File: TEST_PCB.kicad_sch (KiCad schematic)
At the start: 21 parts, among them J101 Conn_01x07_Socket, J102 Conn_01x04_Socket, J103 Conn_01x04_Socket, J104 Conn_01x02_Socket, J105 Conn_01x04_Socket, J106 Conn_01x02_Socket, J107 Conn_01x04_Socket, J108 Conn_01x02_Socket, J109 Conn_01x02_Socket, J110 Conn_01x02_Socket, J111 Conn_01x04_Socket, J112 Conn_01x02_Socket, J113 Conn_01x04_Socket

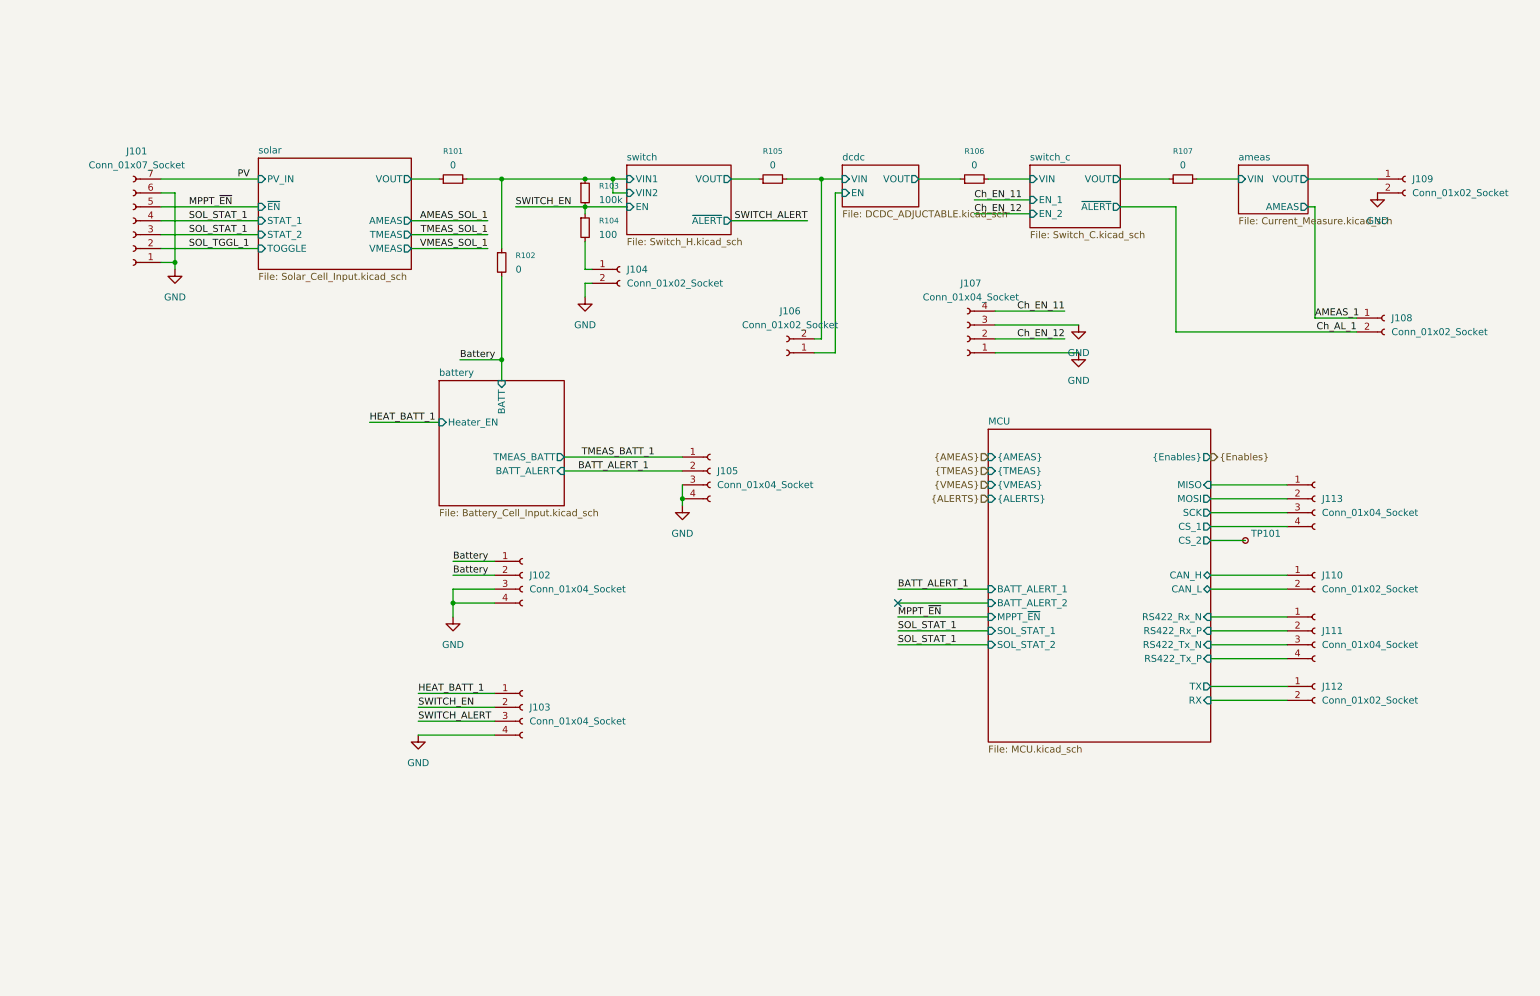
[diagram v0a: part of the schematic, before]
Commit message: reduced number of DCDC converter for PV panels; updated test pcb
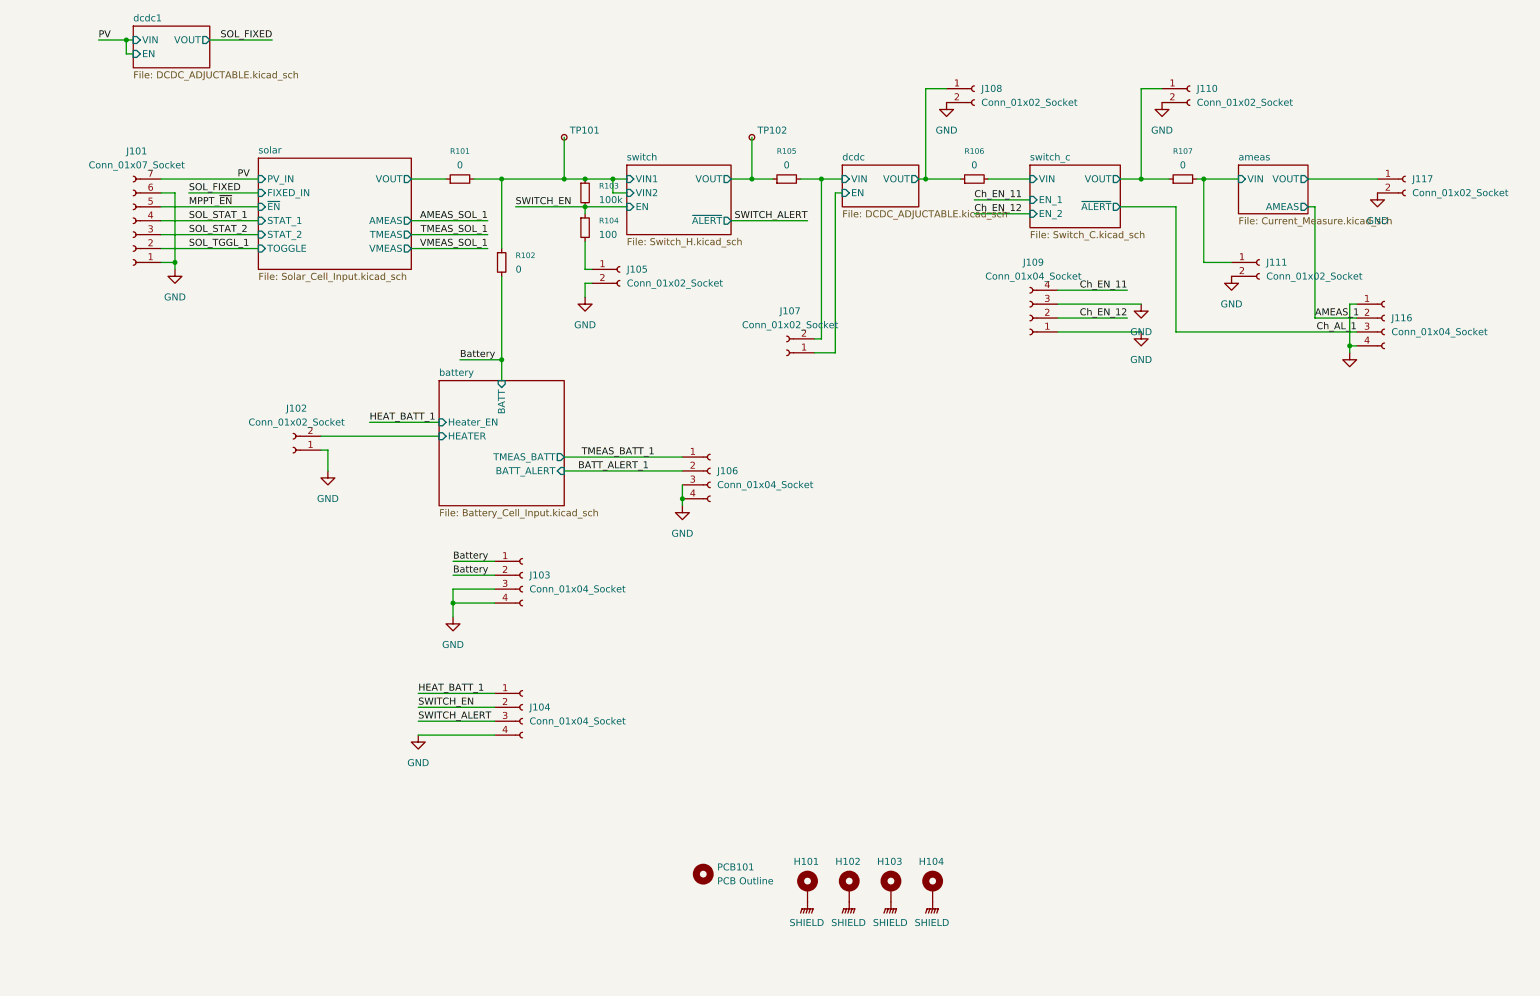
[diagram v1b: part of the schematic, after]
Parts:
- removed J111, J113: Conn_01x04_Socket, symbol Connector:Conn_01x04_Socket
- removed J112: Conn_01x02_Socket, symbol Connector:Conn_01x02_Socket
- added H101, H102, H103, H104: MountingHole, MountingHole:MountingHole_3.2mm_M3_Pad_Via, symbol Mechanical:MountingHole_Pad
- added J102, J111: Conn_01x02_Socket, Connector_PinSocket_2.54mm:PinSocket_1x02_P2.54mm_Vertical, symbol Connector:Conn_01x02_Socket
- added J116: Conn_01x04_Socket, Connector_PinSocket_2.54mm:PinSocket_1x04_P2.54mm_Vertical, symbol Connector:Conn_01x04_Socket
- added PCB101: PCB Outline, Outlines:SPACEMANIC_V1c, symbol Mechanical:MountingHole
- added TP102: ~, TestPoint:TestPoint_Pad_1.0x1.0mm, symbol Connector:TestPoint_Small
- J101: footprint (none) -> Connector_PinSocket_2.54mm:PinSocket_1x07_P2.54mm_Vertical
- J103: renamed from J102; footprint (none) -> Connector_PinSocket_2.54mm:PinSocket_1x04_P2.54mm_Vertical
- J104: renamed from J103; footprint (none) -> Connector_PinSocket_2.54mm:PinSocket_1x04_P2.54mm_Vertical
- J105: renamed from J104; footprint (none) -> Connector_PinSocket_2.54mm:PinSocket_1x02_P2.54mm_Vertical
- J106: renamed from J105; footprint (none) -> Connector_PinSocket_2.54mm:PinSocket_1x04_P2.54mm_Vertical
- J107: renamed from J106; footprint (none) -> Connector_PinSocket_2.54mm:PinSocket_1x02_P2.54mm_Vertical
- J108, J110: footprint (none) -> Connector_PinSocket_2.54mm:PinSocket_1x02_P2.54mm_Vertical
- J109: renamed from J107; footprint (none) -> Connector_PinSocket_2.54mm:PinSocket_1x04_P2.54mm_Vertical
- J117: renamed from J109; footprint (none) -> Connector_PinSocket_2.54mm:PinSocket_1x02_P2.54mm_Vertical
- R101, R102, R103, R104, R105, R106, R107: footprint (none) -> Resistor_SMD:R_0603_1608Metric_Pad0.98x0.95mm_HandSolder
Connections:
- net MCU/CAN_H is gone; now on net switch_c/VOUT: J110.1 (Pin_1)
- net MCU/CAN_L is gone; now on net GND: J110.2 (Pin_2)
- net MCU/CS_2 is gone; now on net switch/VIN1: TP101.1
- net AMEAS_1: now also J116.2 (Pin_2); no longer J108.1 (Pin_1)
- net Ch_AL_1: now also J116.3 (Pin_3); no longer J108.2 (Pin_2)
- net GND: now also J108.2 (Pin_2), J102.1 (Pin_1), J111.2 (Pin_2), J116.1 (Pin_1), J116.4 (Pin_4)
- net SOL_STAT_1: no longer J101.3 (Pin_3)
- net ameas/VIN: now also J111.1 (Pin_1)
- net dcdc/VOUT: now also J108.1 (Pin_1)
- net switch/VOUT: now also TP102.1
- new net SHIELD: H101.1, H102.1, H103.1, H104.1
- new net SOL_STAT_2: J101.3 (Pin_3)
- new net battery/HEATER: J102.2 (Pin_2)
- no-connect marks 1 -> 0
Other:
- removed sheet MCU
- added sheet dcdc1 (DCDC_ADJUCTABLE.kicad_sch)
- sheet battery ports: added HEATER; removed none
- sheet solar ports: added FIXED_IN; removed none
- moved on the sheet: J109, R101, R105

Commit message: restructurization of the entire project improved
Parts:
- removed J101: Conn_01x07_Socket, Connector_PinSocket_2.54mm:PinSocket_1x07_P2.54mm_Vertical, symbol Connector:Conn_01x07_Socket
- removed J102, J107: Conn_01x02_Socket, Connector_PinSocket_2.54mm:PinSocket_1x02_P2.54mm_Vertical, symbol Connector:Conn_01x02_Socket
- removed J103, J109, J116: Conn_01x04_Socket, Connector_PinSocket_2.54mm:PinSocket_1x04_P2.54mm_Vertical, symbol Connector:Conn_01x04_Socket
- removed R106, R107: 0, Resistor_SMD:R_0603_1608Metric_Pad0.98x0.95mm_HandSolder, symbol Device:R_Small
- removed TP101, TP102: ~, TestPoint:TestPoint_Pad_1.0x1.0mm, symbol Connector:TestPoint_Small
- added C101, C104: 1u, Capacitor_SMD:C_0603_1608Metric_Pad1.08x0.95mm_HandSolder, symbol Device:C_Small
- added C102, C103, C105: 100n, Capacitor_SMD:C_0603_1608Metric_Pad1.08x0.95mm_HandSolder, symbol Device:C_Small
- added H105, H106, H107, H108: MountingHole, MountingHole:MountingHole_3.2mm_M3_Pad_TopBottom, symbol Mechanical:MountingHole_Pad
- added J101, J105, J110, J118: Conn_01x03_Pin, Connector_PinHeader_2.54mm:PinHeader_1x03_P2.54mm_Vertical, symbol Connector:Conn_01x03_Pin
- added J102, J137: Conn_01x05_Socket, Connector_PinSocket_2.54mm:PinSocket_1x05_P2.54mm_Vertical, symbol Connector:Conn_01x05_Socket
- added J103, J106, J108, J109, J112, J113, J114, J115, J119, J121, J124, J125, J138, J139, J140, J141, J142: Conn_01x02_Socket, Connector_PinSocket_2.54mm:PinSocket_1x02_P2.54mm_Vertical, symbol Connector:Conn_01x02_Socket
- added J116, J126, J127, J128, J129, J130, J131, J134, J135, J136: Conn_01x02_Pin, Connector_PinHeader_2.54mm:PinHeader_1x02_P2.54mm_Vertical, symbol Connector:Conn_01x02_Pin
- added J132, J133: Conn_01x03_Socket, Connector_PinSocket_2.54mm:PinSocket_1x03_P2.54mm_Vertical, symbol Connector:Conn_01x03_Socket
- added PCB102: PCB Outline, Outlines:SPACEMANIC_V1c, symbol Mechanical:MountingHole
- added Q101: IRLML5103, Package_TO_SOT_SMD:SOT-23-3, symbol Simulation_SPICE:NMOS
- added R103: 100k, Resistor_SMD:R_0603_1608Metric_Pad0.98x0.95mm_HandSolder, symbol Device:R_Small
- added R104: 1k, Resistor_SMD:R_0603_1608Metric_Pad0.98x0.95mm_HandSolder, symbol Device:R_Small
- added U101: LP38690SDX-3.3/NOPB, Package_SON:WSON-6-1EP_3x3mm_P0.95mm, symbol Regulator_Linear:LP38691SD-3.3
- H101, H102, H103, H104: footprint MountingHole:MountingHole_3.2mm_M3_Pad_Via -> MountingHole:MountingHole_3.2mm_M3_Pad_TopBottom
- R101: value 0 -> 10
- R102: value 0 -> 100k
- R105: footprint Resistor_SMD:R_0603_1608Metric_Pad0.98x0.95mm_HandSolder -> Resistor_SMD:R_1210_3225Metric_Pad1.30x2.65mm_HandSolder; now not fitted
- renumbered J106 to J107, J105 to J111, J108 to J117, J110 to J120, J111 to J122, J117 to J123, R103 to R109, R104 to R110
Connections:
- net BATT_ALERT_1 is gone; now on net GND: J107.2 (Pin_2)
- net HEAT_BATT_1 is gone; now on net battery/HEATER: J104.1 (Pin_1)
- net AMEAS_1: now also J124.1 (Pin_1)
- net Battery: now also R105.1, J130.2 (Pin_2), J140.2 (Pin_2); no longer R102.2
- net Ch_AL_1: now also J121.1 (Pin_1)
- net Ch_EN_11: now also J118.1 (Pin_1)
- net Ch_EN_12: now also J118.3 (Pin_3)
- net GND: now also J104.2 (Pin_2), R102.1, C101.2, C102.2, C103.2, C104.2, C105.2, J101.1 (Pin_1), J102.1 (Pin_1), J102.2 (Pin_2), J102.3 (Pin_3), J102.4 (Pin_4), J102.5 (Pin_5), J103.2 (Pin_2), J105.1 (Pin_1), J106.2 (Pin_2), J108.2 (Pin_2), J109.2 (Pin_2), J112.2 (Pin_2), J113.2 (Pin_2), J114.2 (Pin_2), J115.2 (Pin_2), J119.2 (Pin_2), J121.2 (Pin_2), J124.2 (Pin_2), J125.2 (Pin_2), J133.1 (Pin_1), J133.2 (Pin_2), J133.3 (Pin_3), J138.2 (Pin_2), J140.1 (Pin_1), J141.2 (Pin_2), J142.2 (Pin_2), Q101.1 (D), U101.2 (GND), U101.7 (EP); no longer J107.3 (Pin_3)
- net MPPT_~{EN}: now also J105.2 (Pin_2)
- net PV: now also J137.5 (Pin_5)
- net SHIELD: now also H105.1, H106.1, H107.1, H108.1
- net SOL_STAT_1: now also J137.3 (Pin_3)
- net SOL_STAT_2: now also J137.2 (Pin_2)
- net SWITCH_ALERT: now also J115.1 (Pin_1); no longer J104.3 (Pin_3)
- net ameas/VIN: now also J129.1 (Pin_1)
- net dcdc/EN: now also J116.1 (Pin_1)
- net dcdc/VIN: now also J116.2 (Pin_2), J126.1 (Pin_1); no longer R105.2
- net dcdc/VOUT: now also J128.2 (Pin_2), J134.1 (Pin_1)
- net solar/VOUT: now also J125.1 (Pin_1), J127.2 (Pin_2), J130.1 (Pin_1), J131.1 (Pin_1), J142.1 (Pin_1); no longer R101.1
- net switch/VIN1: now also J112.1 (Pin_1), J127.1 (Pin_1); no longer R101.2, R102.1
- net switch/VOUT: now also J114.1 (Pin_1), J126.2 (Pin_2); no longer R105.1
- net switch_c/VIN: now also J119.1 (Pin_1), J128.1 (Pin_1)
- net switch_c/VOUT: now also J129.2 (Pin_2)
- net SWITCH_EN renamed SW_EN
- net SW_EN: no longer J104.2 (Pin_2)
- net TMEAS_BATT_1 renamed battery/TMEAS
- new net: Q101.3 (S), R104.1
- new net: C103.1, C104.1, C105.1, J135.2 (Pin_2), U101.4 (OUT), U101.5 (SNS)
- new net: Q101.2 (G), R101.1, R102.2
- new net +3V3: J135.1 (Pin_1)
- new net +5V: C101.1, C102.1, J101.3 (Pin_3), J103.1 (Pin_1), J105.3 (Pin_3), J110.2 (Pin_2), J118.2 (Pin_2), J134.2 (Pin_2), J141.1 (Pin_1), U101.1 (IN), U101.6 (IN)
- new net SCL: J139.2 (Pin_2)
- new net SDA: J139.1 (Pin_1)
- new net SOL_TGGL: J101.2 (Pin_2), J137.1 (Pin_1), R101.2
- new net ameas1/AMEAS: J113.1 (Pin_1)
- new net battery/ALERT: J107.3 (Pin_3)
- new net battery/BATT: R105.2
- new net battery/Heater_EN: J104.3 (Pin_3)
- new net dcdc1/VOUT: J136.2 (Pin_2)
- new net solar/AMEAS: J132.1 (Pin_1)
- new net solar/CC_Source: J138.1 (Pin_1)
- new net solar/TMEAS: J132.2 (Pin_2)
- new net solar/VMEAS: J132.3 (Pin_3)
- new net switch1/EN: R103.1, R104.2
- new net switch1/PG: J106.1 (Pin_1)
- new net switch1/VIN1: J136.1 (Pin_1), R103.2
- new net switch1/VOUT: J108.1 (Pin_1), J131.2 (Pin_2)
- new net switch_c1/EN_1: J110.1 (Pin_1)
- new net switch_c1/EN_2: J110.3 (Pin_3)
- new net switch_c1/PG: J109.1 (Pin_1)
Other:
- added sheet ameas1 (Current_Measure.kicad_sch)
- added sheet switch1 (Switch_H.kicad_sch)
- added sheet switch_c1 (Switch_C.kicad_sch)
- sheet battery ports: added ALERT, TMEAS; removed BATT_ALERT, TMEAS_BATT
- sheet solar ports: added CC_Source; removed FIXED_IN
- sheet switch ports: added PG; removed ~{ALERT}
- sheet switch_c ports: added PG; removed ~{ALERT}
- moved on the sheet: H101, H102, H103, H104, J107, J111, J117, J120, J122, J123, PCB101, R109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
